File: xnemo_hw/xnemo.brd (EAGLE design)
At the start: 49.8 x 49.8 mm, 60 parts, among them J1 MICRO_USB_B_RECEPT, J2 DM3D_MICRO_SD, J3 HEADER_2X5_0.05_SMD, J4 HEADER_2X7, J5 HEADER_2X7, J7 HEADER_2X7, U1 LTC3559, U10 STTS751, U2 L3GD20, U4 STM32F407VE, U7 LSM303DLHC, U8 LSM303DLHC, U9 L3GD20, X1 TXC_7A_XTAL

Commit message: All connections made -- no DRC yet
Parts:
- J7: value HEADER_2X7 -> HEADER_2X8; device xnemo:HEADER_2X7_0.05X0.1_THRU -> xnemo:HEADER_2X8_0.05X0.1_THRU
- moved C13 16.3 mm to (16.0, 23.5), turned to 180 degrees
- moved C24 9.12 mm to (34.0, 3.33), flipped to the top, turned to 90 degrees
- moved U2 3.56 mm to (11.7, 6.03)
- moved C25 3.29 mm to (38.3, 6.11), turned to 0 degrees
- moved C1 3.15 mm to (11.7, 1.98)
- moved C23 1.28 mm to (31.5, 2.70), turned to 180 degrees
- moved C17 1.23 mm to (18.3, 13.0), turned to 90 degrees
- moved C21 1.11 mm to (24.9, 7.94)
- moved LED3 0.40 mm to (45.1, 18.5)
- moved LED2 0.40 mm to (41.7, 18.5)
- moved LED1 0.35 mm to (38.2, 18.5)
- moved C9 0.32 mm to (7.38, 18.5)
- moved R11 0.24 mm to (38.2, 21.6)
- moved R13 0.24 mm to (45.1, 21.6)
- moved SB2 0.24 mm to (9.68, 18.5)
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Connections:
- removed net I2S3_WS: U4.P$77
- removed net N$8: LED1.C, LED2.C, LED3.C
- net GND: now also LED1.C, LED2.C, LED3.C
- net USART2_RX: now also J7.16
- net USART2_TX: now also J7.15
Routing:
- net 3V3: track 197.3 -> 316.4 mm, vias 12 -> 16
- net VBAT: track 24.4 -> 65.2 mm, vias 3 -> 6
- net DCMI_D0_MCK: track 25.0 -> 65.4 mm, vias 1 -> 4
- net I2C2_SCL: track 29.1 -> 64.5 mm, vias 1 -> 3
- net I2C2_SDA: track 29.6 -> 65.0 mm, vias 1 -> 2
- net PE11: track 0.00 -> 35.4 mm, vias 0 -> 3
- net USART2_TX: track 0.00 -> 33.6 mm, vias 0 -> 1
- net SD_DAT0_I2C3_SCL: track 24.8 -> 57.4 mm, vias 1 -> 4
- net SD_DAT1_I2C3_SDA: track 24.6 -> 55.2 mm, vias 1 -> 4
- net USART2_RX: track 0.00 -> 24.2 mm, vias 0 -> 2
- net PB1: track 0.00 -> 22.3 mm
- net PB0: track 0.00 -> 21.1 mm
- net PC5: track 0.00 -> 19.9 mm
- net PC4: track 0.00 -> 18.8 mm
- net PA7: track 0.00 -> 17.6 mm
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
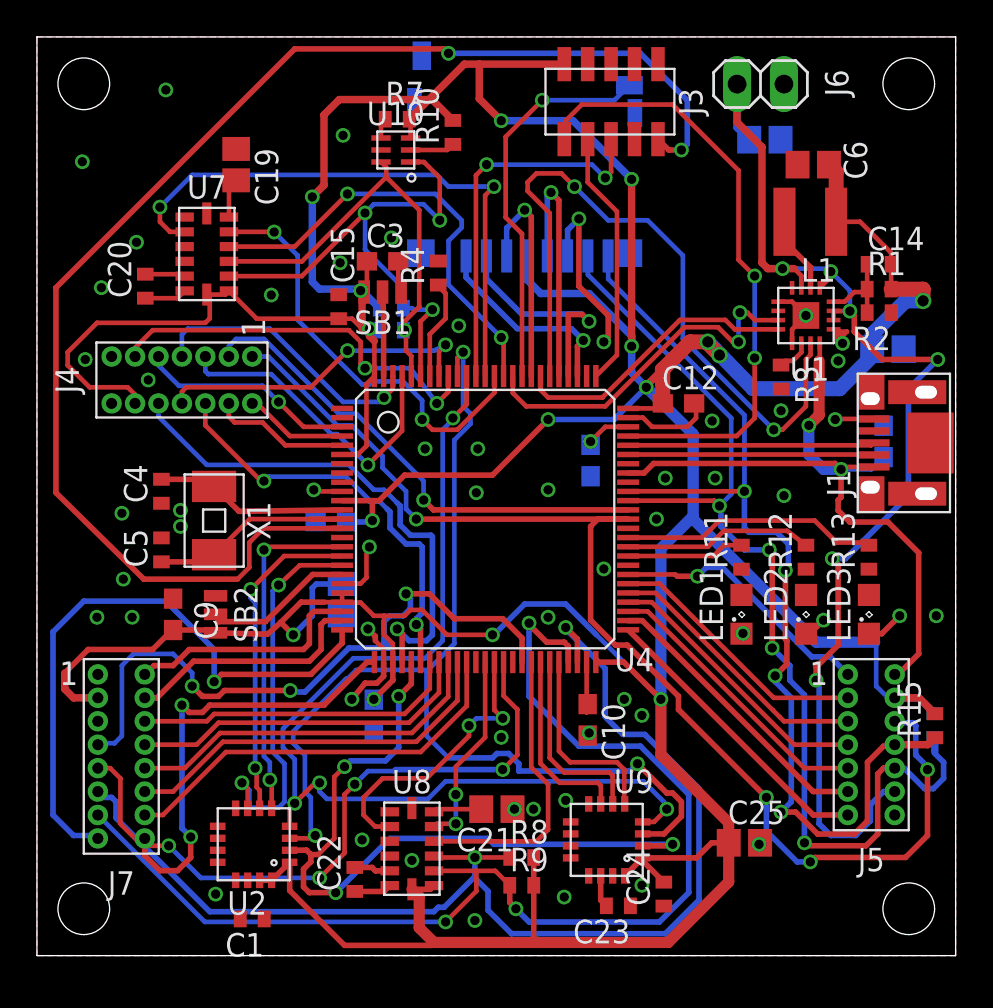
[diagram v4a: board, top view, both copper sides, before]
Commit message: Added microphone, DRC passed, no airwires
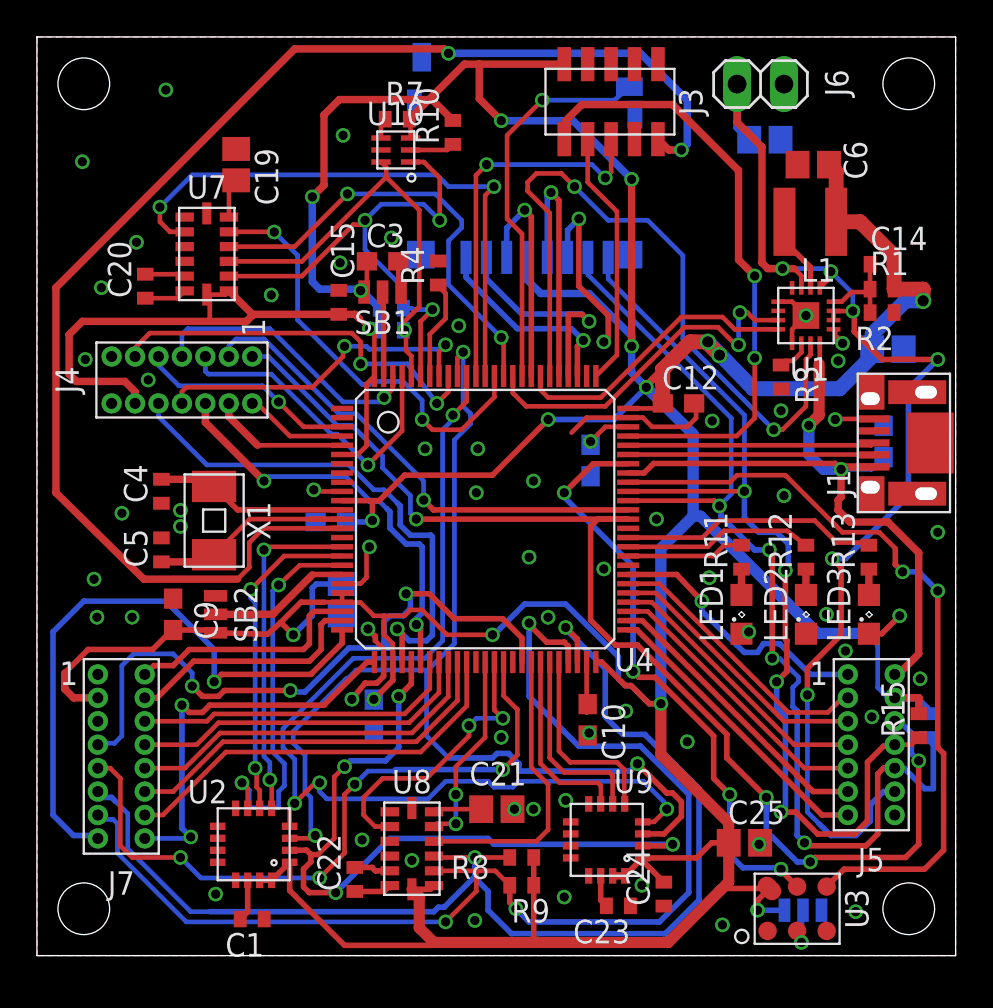
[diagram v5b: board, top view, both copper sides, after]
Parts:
- added SB3: SOLDER_BRIDGE_2, xnemo:SOLDER_BRIDGE_2
- added U3: MP45DT02, xnemo:ST_HLGA6
- moved R15 0.87 mm to (47.8, 12.5)
- moved R14 0.40 mm to (48.3, 12.5)
- moved C15 0.24 mm to (16.4, 35.4)
- moved C14 0.16 mm to (45.8, 37.5)
- moved R1 0.16 mm to (45.8, 36.1)
- moved R2 0.16 mm to (45.8, 34.8)
- moved J2 0.08 mm to (27.1, 43.8)
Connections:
- removed net N$3: U4.P$69
- removed net N$5: U4.P$67
- new net MIC_LR: SB3.P$2, U3.2
- new net USART1_CK: U3.4, U4.P$67
- new net USART1_RX: U3.5, U4.P$69
- net 3V3: now also SB3.P$1, U3.6
- net GND: now also SB3.P$3, U3.1, U3.3
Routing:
- net USART1_CK: track 0.00 -> 41.4 mm, vias 0 -> 2
- net USART1_RX: track 0.00 -> 32.4 mm, vias 0 -> 4
- net 3V3: track 316.4 -> 325.0 mm, vias 16 -> 17
- net USART2_RX: track 24.2 -> 21.6 mm
- net MIC_LR: track 0.00 -> 2.50 mm, vias 0 -> 1
- net GYR_RES1: track 0.00 -> 2.39 mm
- net SD_DAT1_I2C3_SDA: track 55.2 -> 53.6 mm
- net N$9: track 0.00 -> 1.40 mm
- net N$17: track 0.00 -> 1.40 mm
- net N$16: track 0.00 -> 1.40 mm
- net GND: track 38.7 -> 39.7 mm, vias 57 -> 62
- net I2C2_SCL: track 64.5 -> 65.5 mm
- net PE9: track 36.6 -> 37.3 mm
- net VBAT: track 65.2 -> 65.9 mm
- net USART3_RX: track 14.5 -> 15.1 mm
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
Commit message: Attempting to genereate CAM files
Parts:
- added C18, C26, C27: 2.2u, resistor:C0603
- moved C1 0.80 mm to (11.7, 2.78)
- moved J3 0.40 mm to (31.1, 45.9)
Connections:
- net 3V3: now also C16.2, C18.2, C26.1, C27.2, J3.1; no longer C16.1, J3.2
- net GND: now also C16.1, C18.1, C26.2, C27.1, J3.3, J3.5, J3.7, J3.9; no longer C16.2, J3.10, J3.4, J3.6, J3.8
- net NC: now also J3.8; no longer J3.7
- net NRESET: now also J3.10; no longer J3.9
- net SWDCLK: now also J3.4; no longer J3.3
- net SWDIO: now also J3.2; no longer J3.1
- net SWO: now also J3.6; no longer J3.5
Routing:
- net SWO: track 20.7 -> 33.6 mm
- net SWDCLK: track 14.0 -> 20.9 mm
- net 3V3: track 325.0 -> 330.3 mm, vias 17 -> 18
- net GND: track 39.7 -> 34.9 mm, vias 62 -> 95
- net NRESET: track 75.5 -> 71.2 mm
- net SWDIO: track 33.3 -> 37.3 mm
- net POW_SUSP: track 19.6 -> 23.5 mm
- net SD_CMD: track 12.1 -> 10.7 mm
- net SD_CLK: track 13.7 -> 12.3 mm
- net GYR_RES1: track 2.39 -> 1.44 mm
- net POW_CHRG: track 38.7 -> 37.8 mm
- net SD_DAT3: track 12.3 -> 11.6 mm
- net SD_DET: track 21.1 -> 21.7 mm
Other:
- board text added: "Gyro:"
- board text added: "Mag/Acc"
- board text added: "x"
- board text added: "y"
- board text added: "z"

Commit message: Fixed missing connection
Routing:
- net GND: vias 95 -> 96
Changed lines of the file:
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@@
 <layer number="23" name="tOrigins" color="15" fill="1" visible="yes" active="yes"/>
 <layer number="24" name="bOrigins" color="15" fill="1" visible="yes" active="yes"/>
-<layer number="25" name="tNames" color="7" fill="1" visible="yes" active="yes"/>
-<layer number="26" name="bNames" color="7" fill="1" visible="yes" active="yes"/>
+<layer number="25" name="tNames" color="7" fill="1" visible="no" active="yes"/>
+<layer number="26" name="bNames" color="7" fill="1" visible="no" active="yes"/>
 <layer number="27" name="tValues" color="7" fill="1" visible="no" active="yes"/>
 <layer number="28" name="bValues" color="7" fill="1" visible="no" active="yes"/>
 <layer number="29" name="tStop" color="7" fill="3" visible="no" active="yes"/>
 <layer number="30" name="bStop" color="7" fill="6" visible="no" active="yes"/>
-<layer number="31" name="tCream" color="7" fill="4" visible="yes" active="yes"/>
-<layer number="32" name="bCream" color="7" fill="5" visible="yes" active="yes"/>
+<layer number="31" name="tCream" color="7" fill="4" visible="no" active="yes"/>
+<layer number="32" name="bCream" color="7" fill="5" visible="no" active="yes"/>
 <layer number="33" name="tFinish" color="6" fill="3" visible="no" active="yes"/>
 <layer number="34" name="bFinish" color="6" fill="6" visible="no" active="yes"/>
-<layer number="35" name="tGlue" color="7" fill="4" visible="yes" active="yes"/>
-<layer number="36" name="bGlue" color="7" fill="5" visible="yes" active="yes"/>
+<layer number="35" name="tGlue" color="7" fill="4" visible="no" active="yes"/>
+<layer number="36" name="bGlue" color="7" fill="5" visible="no" active="yes"/>
 <layer number="37" name="tTest" color="7" fill="1" visible="no" active="yes"/>
 <layer number="38" name="bTest" color="7" fill="1" visible="no" active="yes"/>
@@
 <layer number="43" name="vRestrict" color="2" fill="10" visible="no" active="yes"/>
 <layer number="44" name="Drills" color="7" fill="1" visible="no" active="yes"/>
-<layer number="45" name="Holes" color="7" fill="1" visible="yes" active="yes"/>
-<layer number="46" name="Milling" color="3" fill="1" visible="yes" active="yes"/>
-<layer number="47" name="Measures" color="7" fill="1" visible="yes" active="yes"/>
-<layer number="48" name="Document" color="7" fill="1" visible="yes" active="yes"/>
-<layer number="49" name="Reference" color="7" fill="1" visible="yes" active="yes"/>
-<layer number="51" name="tDocu" color="7" fill="1" visible="yes" active="yes"/>
-<layer number="52" name="bDocu" color="7" fill="1" visible="yes" active="yes"/>
+<layer number="45" name="Holes" color="7" fill="1" visible="no" active="yes"/>
+<layer number="46" name="Milling" color="3" fill="1" visible="no" active="yes"/>
+<layer number="47" name="Measures" color="7" fill="1" visible="no" active="yes"/>
+<layer number="48" name="Document" color="7" fill="1" visible="no" active="yes"/>
+<layer number="49" name="Reference" color="7" fill="1" visible="no" active="yes"/>
+<layer number="51" name="tDocu" color="7" fill="1" visible="no" active="yes"/>
+<layer number="52" name="bDocu" color="7" fill="1" visible="no" active="yes"/>
 <layer number="91" name="Nets" color="2" fill="1" visible="no" active="no"/>
 <layer number="92" name="Busses" color="1" fill="1" visible="no" active="no"/>
@@
 <wire x1="15.581875" y1="19.15375" x2="14.311875" y2="19.15375" width="0.3048" layer="1"/>
 <wire x1="14.311875" y1="19.15375" x2="13.2159375" y2="18.0578125" width="0.3048" layer="1"/>
-<wire x1="13.2159375" y1="18.0578125" x2="12.49375" y2="17.415" width="0.3048" layer="1"/>
-<wire x1="12.49375" y1="17.415" x2="9.68375" y2="17.494375" width="0.3048" layer="1"/>
+<wire x1="13.2159375" y1="18.0578125" x2="12.6525" y2="17.494375" width="0.3048" layer="1"/>
+<wire x1="12.6525" y1="17.494375" x2="9.68375" y2="17.494375" width="0.4064" layer="1"/>
 <wire x1="9.68375" y1="17.494375" x2="9.454375" y2="17.644375" width="0.3048" layer="1"/>
-<wire x1="9.454375" y1="17.644375" x2="7.381875" y2="17.644375" width="0.3048" layer="1"/>
+<wire x1="9.454375" y1="17.644375" x2="7.381875" y2="17.644375" width="0.4064" layer="1"/>
 <wire x1="16.53875" y1="24.65375" x2="18.176875" y2="24.65375" width="0.3048" layer="1"/>
 <wire x1="18.176875" y1="24.65375" x2="18.541875" y2="24.65375" width="0.3048" layer="1"/>
@@
 <wire x1="27.701875" y1="29.05125" x2="31.27375" y2="29.05125" width="0.3048" layer="16"/>
 <wire x1="31.27375" y1="29.05125" x2="33.02" y2="30.7975" width="0.3048" layer="16"/>
-<wire x1="15.1375" y1="20.138125" x2="14.9225" y2="19.923125" width="0.3048" layer="16"/>
-<wire x1="14.9225" y1="19.923125" x2="14.9225" y2="18.415" width="0.3048" layer="16"/>
-<wire x1="14.9225" y1="18.415" x2="13.890625" y2="17.383125" width="0.3048" layer="16"/>
 <via x="13.890625" y="17.383125" extent="1-16" drill="0.5"/>
 <wire x1="13.890625" y1="17.383125" x2="13.2159375" y2="18.0578125" width="0.3048" layer="1"/>
@@
 <wire x1="16.53875" y1="19.65375" x2="16.53875" y2="19.15375" width="0.254" layer="1"/>
 <wire x1="7.381875" y1="17.644375" x2="7.325625" y2="17.644375" width="0.3048" layer="1"/>
-<wire x1="7.325625" y1="17.644375" x2="6.270625" y2="16.589375" width="0.3048" layer="1"/>
-<wire x1="6.270625" y1="16.589375" x2="2.778125" y2="16.589375" width="0.3048" layer="1"/>
-<wire x1="2.778125" y1="16.589375" x2="1.508125" y2="15.319375" width="0.3048" layer="1"/>
+<wire x1="7.325625" y1="17.644375" x2="6.270625" y2="16.589375" width="0.4064" layer="1"/>
+<wire x1="6.270625" y1="16.589375" x2="2.778125" y2="16.589375" width="0.4064" layer="1"/>
+<wire x1="2.778125" y1="16.589375" x2="1.508125" y2="15.319375" width="0.4064" layer="1"/>
 <wire x1="16.804375" y1="23.495" x2="18.0975" y2="23.495" width="0.3048" layer="16"/>
 <wire x1="18.0975" y1="23.495" x2="18.176875" y2="23.574375" width="0.3048" layer="16"/>
@@
 <wire x1="28.575" y1="44.29125" x2="28.575" y2="45.085" width="0.4064" layer="16"/>
 <wire x1="28.575" y1="45.085" x2="28.73375" y2="45.24375" width="0.4064" layer="16"/>
-<wire x1="16.53875" y1="19.15375" x2="16.51" y2="18.438125" width="0" layer="19" extent="1-16"/>
+<wire x1="16.51" y1="18.438125" x2="14.945625" y2="18.438125" width="0.4064" layer="16"/>
+<wire x1="14.945625" y1="18.438125" x2="13.890625" y2="17.383125" width="0.4064" layer="16"/>
 </signal>
 <signal name="GND">
@@
 <via x="17.065625" y="13.890625" extent="1-16" drill="0.5"/>
 <via x="25.87625" y="7.9375" extent="1-16" drill="0.5"/>
-<via x="17.62125" y="6.270625" extent="1-16" drill="0.5"/>
+<via x="17.541875" y="6.429375" extent="1-16" drill="0.5"/>
 <wire x1="16.53875" y1="20.15375" x2="17.534375" y2="20.15375" width="0.254" layer="1"/>
 <wire x1="17.534375" y1="20.15375" x2="17.859375" y2="20.47875" width="0.254" layer="1"/>
@@
 <via x="47.863125" y="15.001875" extent="1-16" drill="0.5"/>
 <via x="37.1475" y="1.666875" extent="1-16" drill="0.5"/>
-<via x="44.370625" y="2.38125" extent="1-16" drill="0.5"/>
+<via x="45.481875" y="1.11125" extent="1-16" drill="0.5"/>
 <via x="26.67" y="21.59" extent="1-16" drill="0.5"/>
 <via x="35.2425" y="11.58875" extent="1-16" drill="0.5"/>
@@
 <via x="1.825625" y="8.969375" extent="1-16" drill="0.5"/>
 <via x="9.04875" y="7.858125" extent="1-16" drill="0.5"/>
+<via x="45.24375" y="3.81" extent="1-16" drill="0.5"/>
 </signal>
 <signal name="GYR_RES1">
@@
 <wire x1="35.004375" y1="49.291875" x2="28.813125" y2="49.291875" width="0.4064" layer="1"/>
 <wire x1="28.813125" y1="49.291875" x2="28.575" y2="49.05375" width="0.4064" layer="1"/>
-<wire x1="28.575" y1="49.05375" x2="28.575" y2="47.863125" width="0.4064" layer="1"/>
-<wire x1="28.575" y1="47.863125" x2="28.575" y2="47.91075" width="0" layer="19" extent="1-1"/>
+<wire x1="28.575" y1="49.05375" x2="28.575" y2="47.91075" width="0.4064" layer="1"/>
+<wire x1="28.575" y1="47.91075" x2="28.575" y2="47.863125" width="0.4064" layer="1"/>
 </signal>
 <signal name="SWDCLK">
